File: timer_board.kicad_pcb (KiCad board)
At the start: 2 copper layers, 127 x 76.2 mm, 54 parts, among them CON1 AVR-ISP-6, IC1 ATMEGA32U4, K1 T9AS5D22-5, P1 USBMICRO, P2 OUT_INV, P3 Trigger, P4 OUT, Q1 NPN, Q2 NPN, U1 DS3231MZ, U2 74HC04, Y1 RESONATORSMD

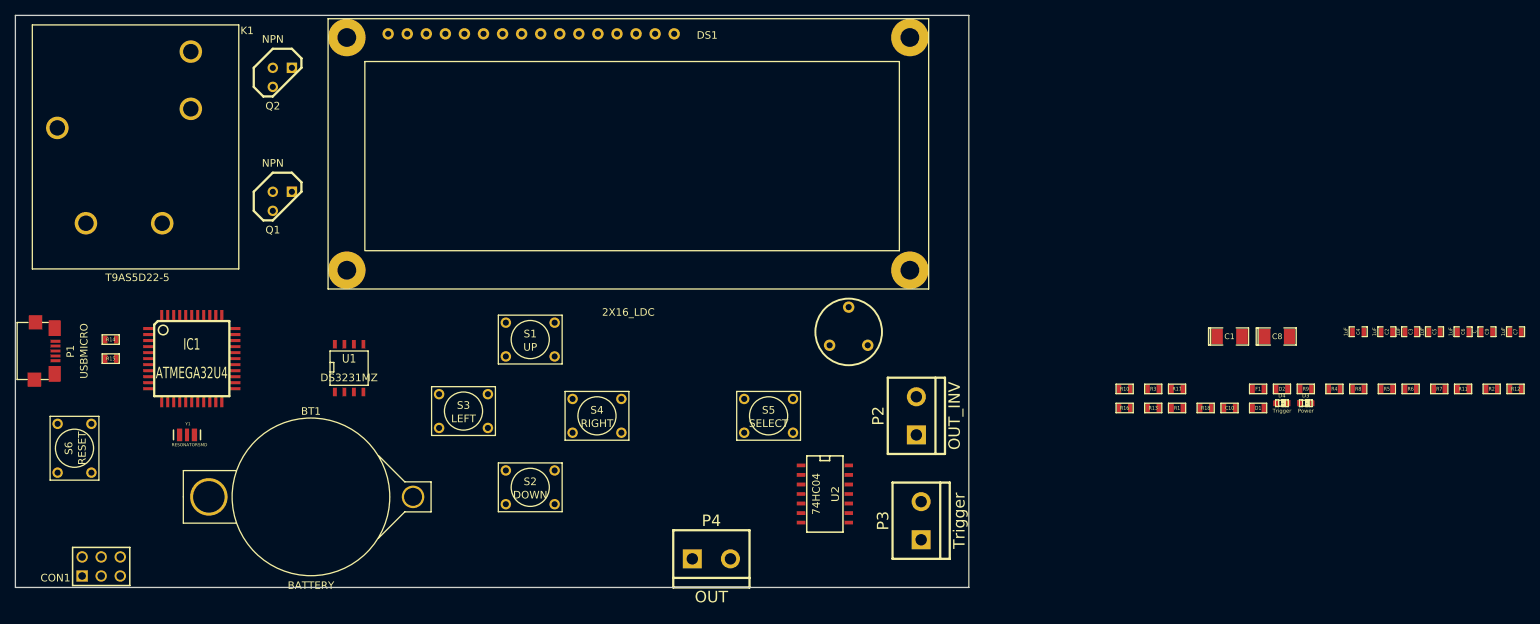
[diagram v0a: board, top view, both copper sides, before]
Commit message: Moved stuff arround so every thing fits in outline
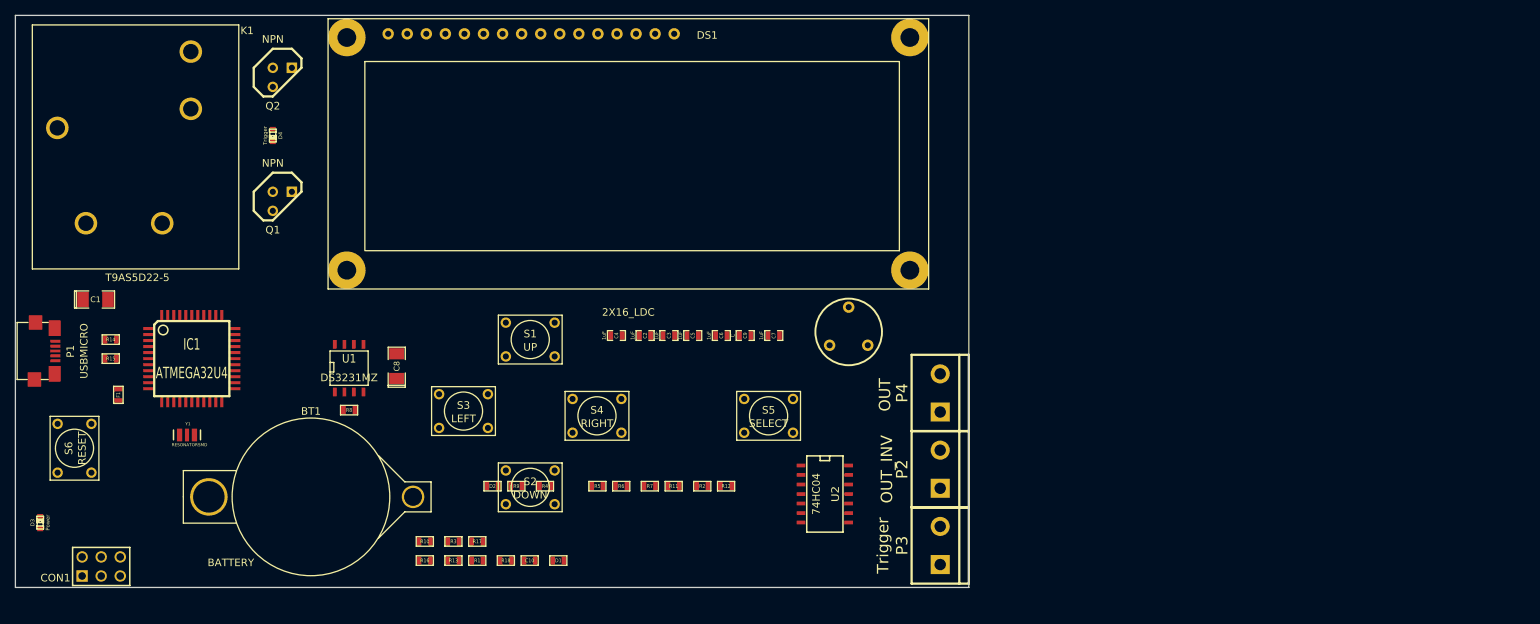
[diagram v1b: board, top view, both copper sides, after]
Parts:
- moved D3 169.3 mm to (28.7, 93.0), turned to 90 degrees
- moved F1 151.8 mm to (39.1, 75.9), turned to 90 degrees
- moved C1 151.1 mm to (36.1, 63.2)
- moved D4 139.1 mm to (59.7, 41.4), turned to 270 degrees
- moved R8 134.4 mm to (69.8, 78.0)
- moved C8 117.3 mm to (76.2, 72.1), turned to 90 degrees
- moved D2 106.0 mm to (89.0, 88.1)
- moved R11 106.0 mm to (113.1, 88.1)
- moved R2 106.0 mm to (116.9, 88.1)
- moved R4 106.0 mm to (95.9, 88.1)
- moved R5 106.0 mm to (102.9, 88.1)
- moved R12 106.0 mm to (120.1, 88.1)
- moved R6 106.0 mm to (106.1, 88.1)
- moved R7 106.0 mm to (109.9, 88.1)
- moved R9 106.0 mm to (92.1, 88.1)
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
